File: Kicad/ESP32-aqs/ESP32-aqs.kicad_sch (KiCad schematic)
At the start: 22 parts, among them J1 UART Connector, SW1 RESET, SW2 BOOT, U1 LD1117S33TR_SOT223, U2 ESP32-WROOM-32, U3 SGP41-D-R4, U4 SX1276S8S+T-X1

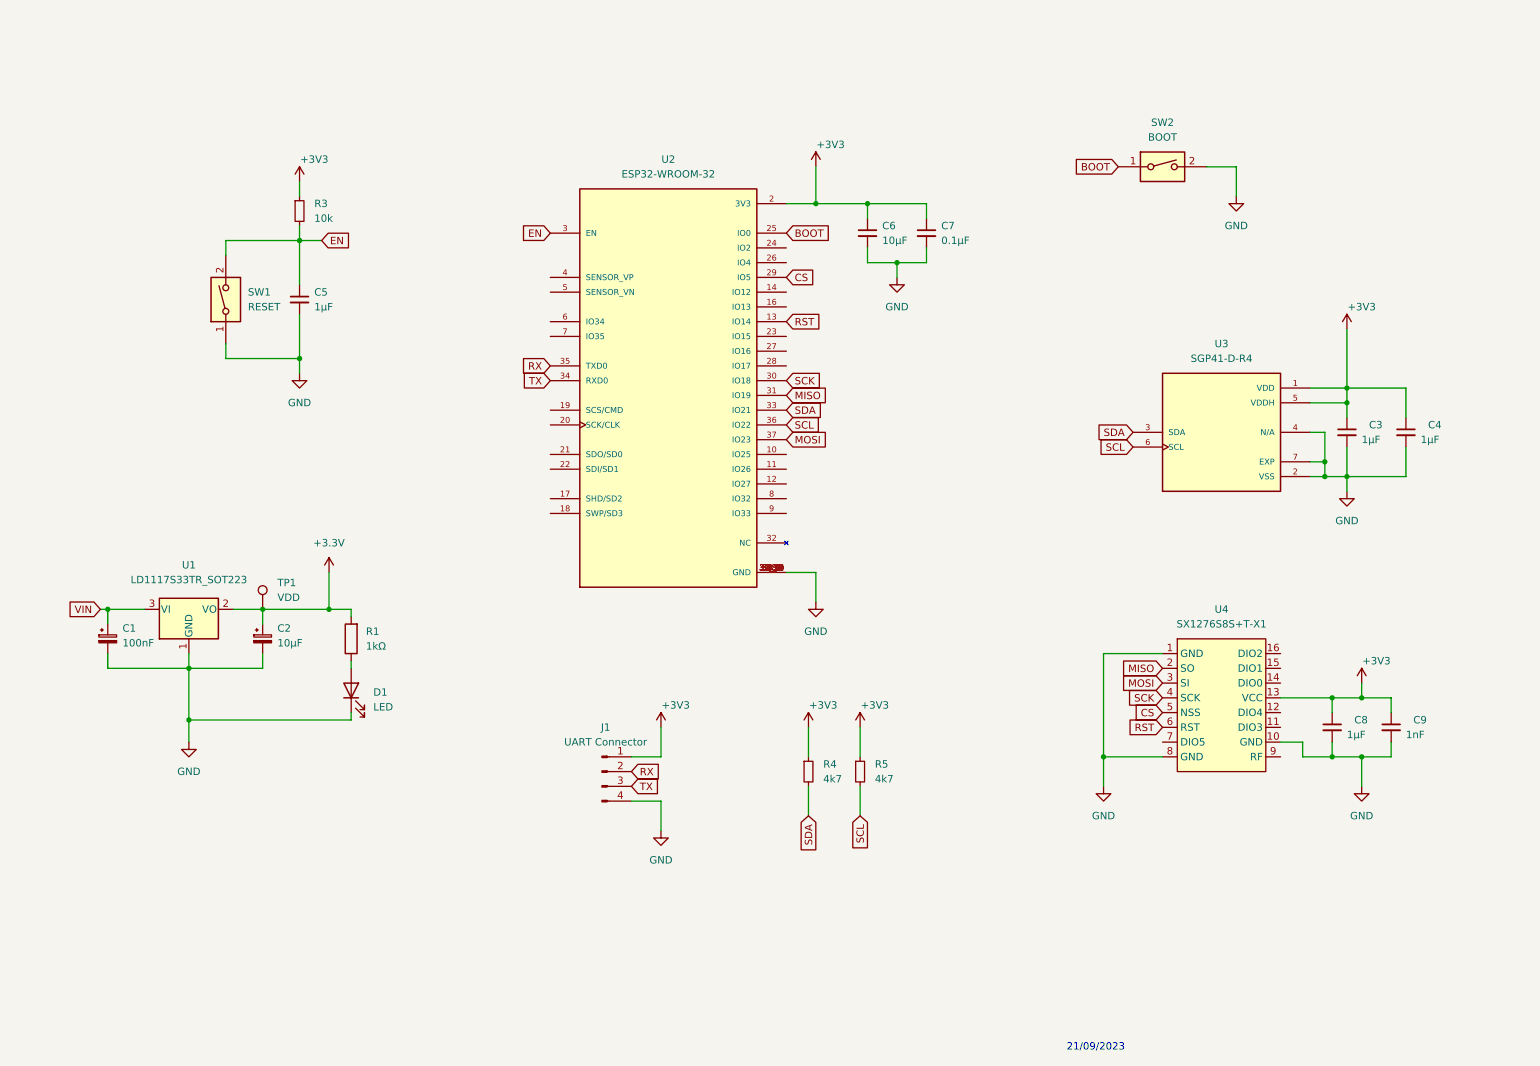
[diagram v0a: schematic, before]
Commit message: update schematic
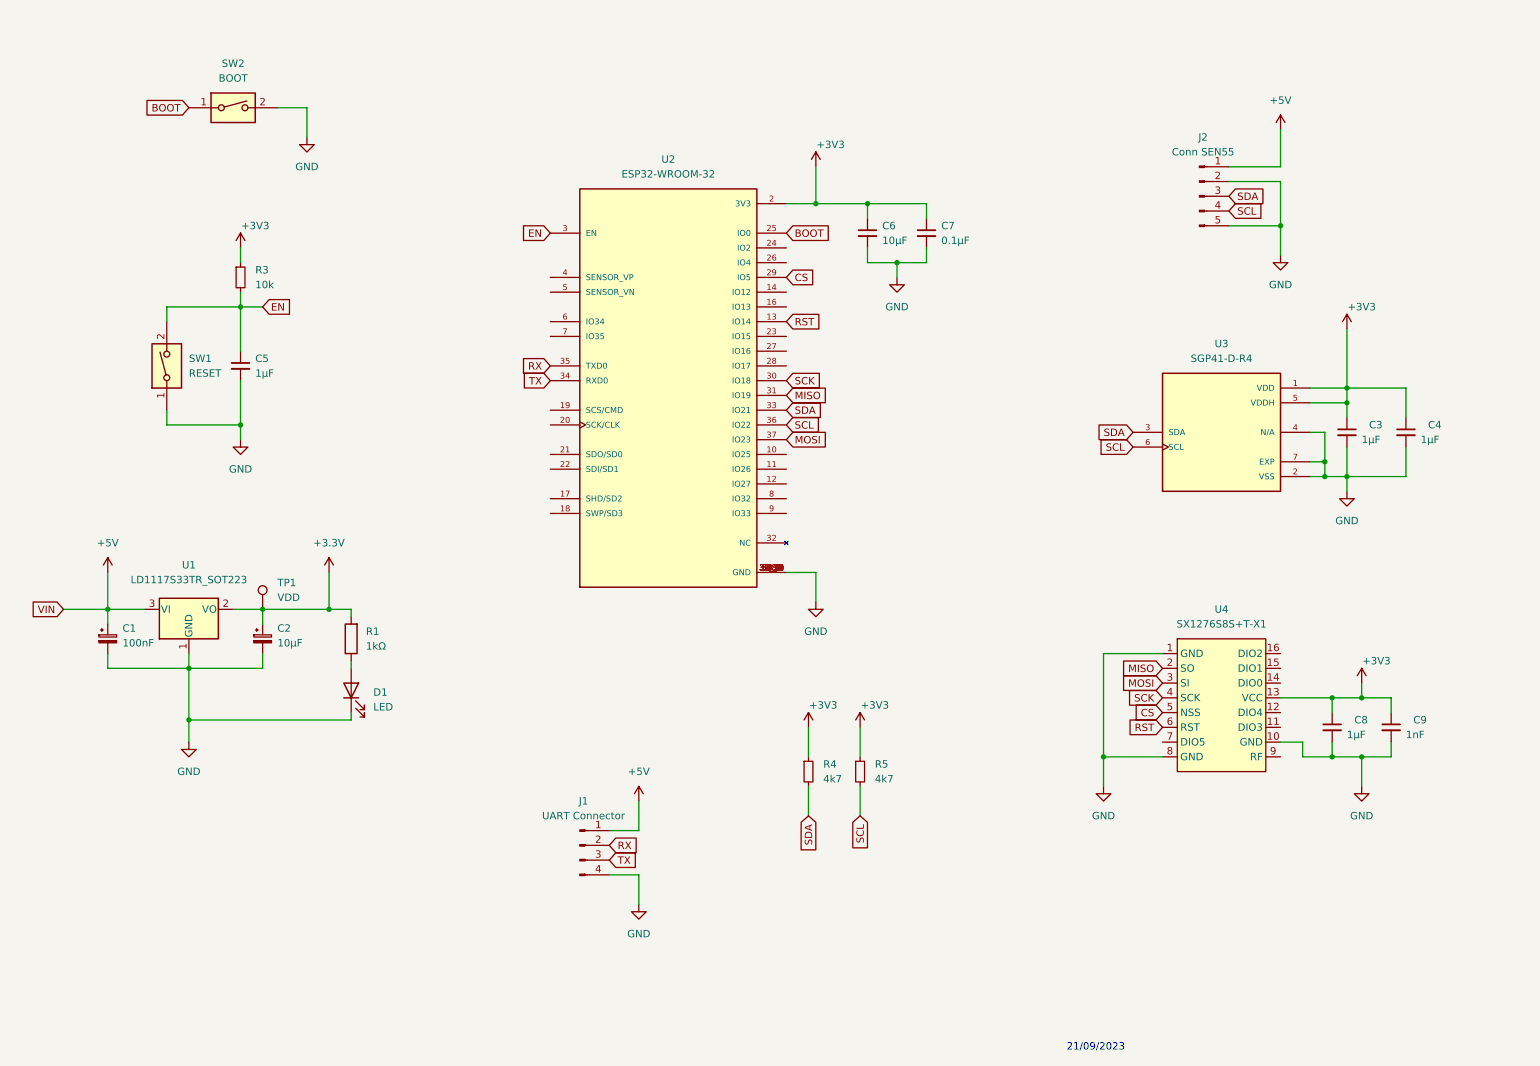
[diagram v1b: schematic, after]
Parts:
- added J2: Conn SEN55, Connector_PinHeader_2.54mm:PinHeader_1x05_P2.54mm_Vertical, symbol Connector:Conn_01x05_Male
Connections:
- net +3V3: no longer J1.1 (Pin_1)
- net GND: now also J2.2 (Pin_2), J2.5 (Pin_5)
- net SCL: now also J2.4 (Pin_4)
- net SDA: now also J2.3 (Pin_3)
- net VIN renamed +5V
- net +5V: now also J1.1 (Pin_1), J2.1 (Pin_1)
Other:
- moved on the sheet: C5, J1, R3, SW1, SW2

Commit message: Add files via upload
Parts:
- added J3: ufl connector, Connector_Coaxial:U.FL_Molex_MCRF_73412-0110_Vertical, symbol Connector:Conn_Coaxial
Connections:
- net GND: now also J3.2 (Ext)
- net at U4.9 (RF): now also J3.1 (In)
- no-connect marks 0 -> 28
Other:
- moved on the sheet: C1, C2, C5, C6, C7, C8, C9, D1, R1, R3, SW1, SW2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

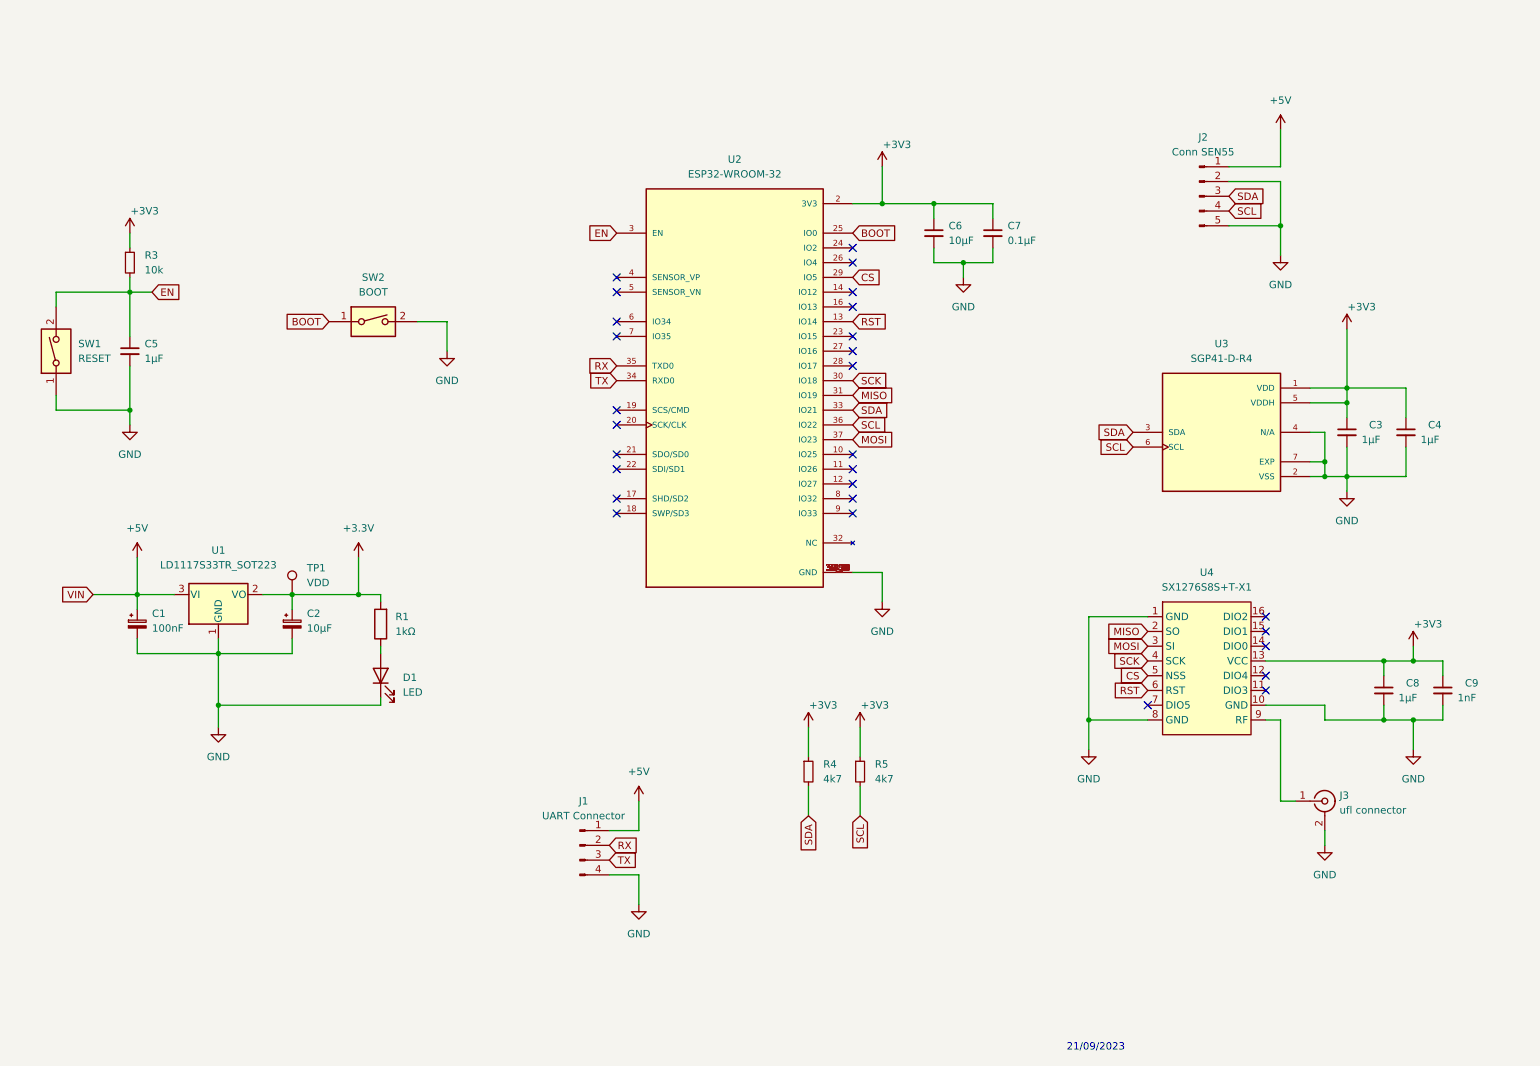
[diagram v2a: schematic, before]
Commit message: update schematic
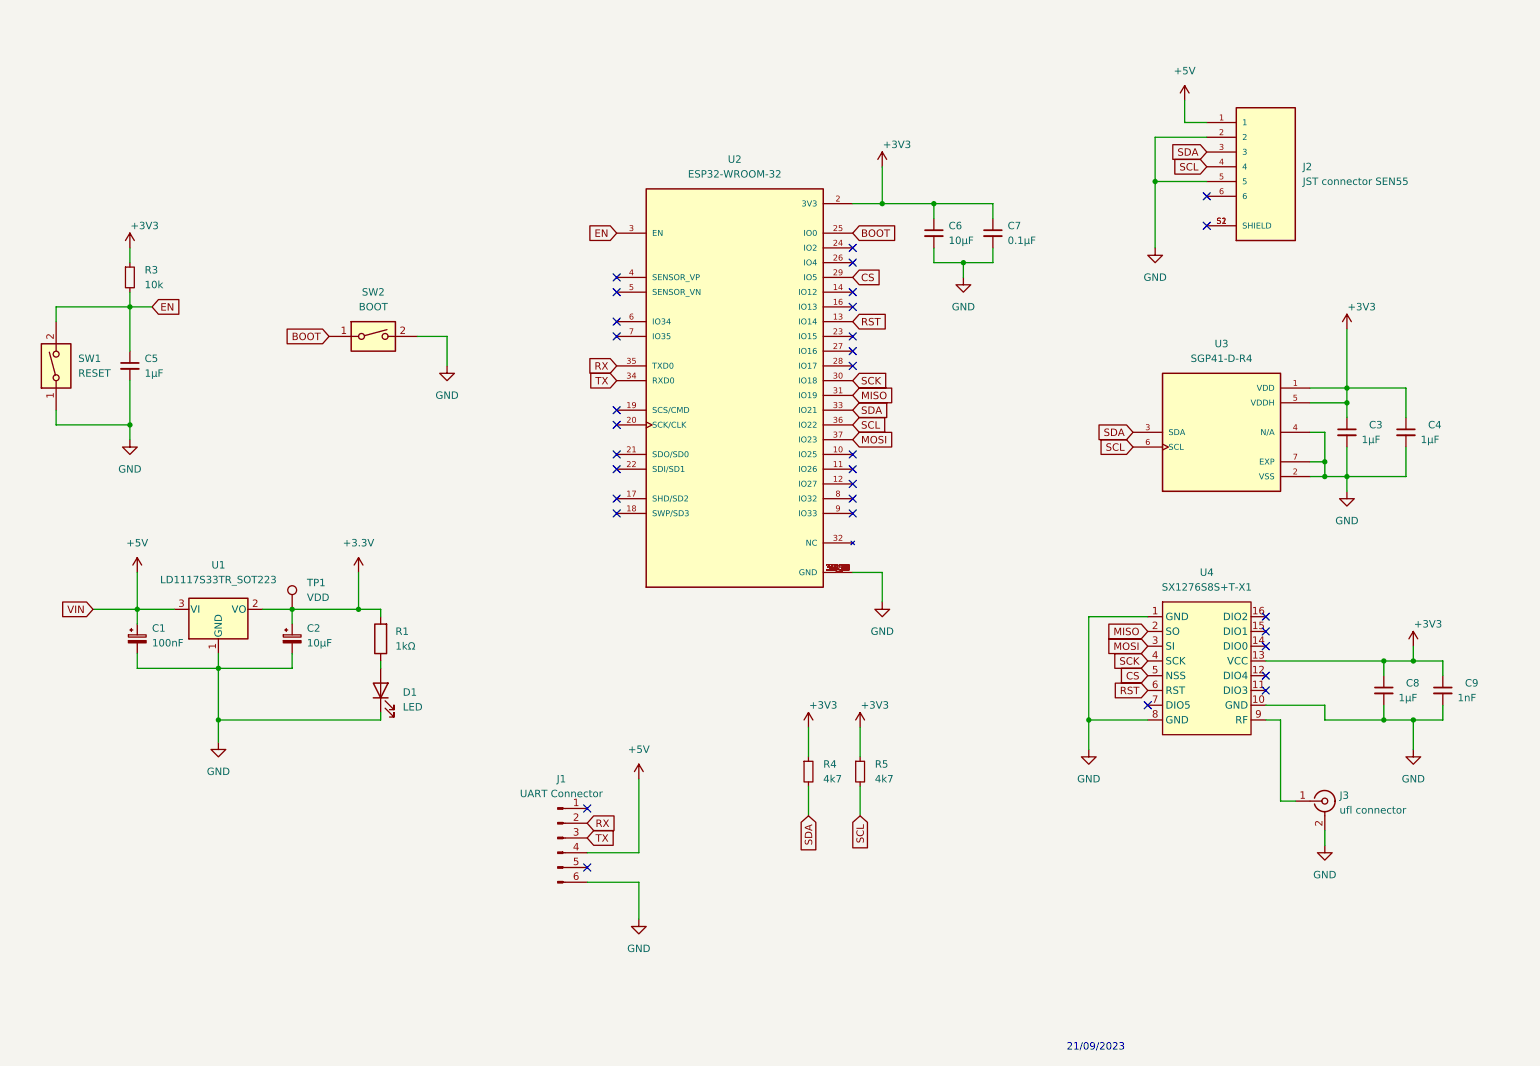
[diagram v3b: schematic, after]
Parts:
- removed J1: UART Connector, Connector_PinHeader_2.54mm:PinHeader_1x04_P2.54mm_Vertical, symbol Connector:Conn_01x04_Male
- removed J2: Conn SEN55, Connector_PinHeader_2.54mm:PinHeader_1x05_P2.54mm_Vertical, symbol Connector:Conn_01x05_Male
- added J1: UART Connector, Connector_PinHeader_2.54mm:PinHeader_1x06_P2.54mm_Vertical, symbol Connector:Conn_01x06_Male
- added J2: JST connector SEN55, ESP32-aqs:JST_BM06B-GHS-TBT_LF__SN__N_, symbol ESP32-aqs:BM06B-GHS-TBT_LF__SN__N_
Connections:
- net +5V: now also J1.4 (Pin_4), J2.1
- net GND: now also J1.6 (Pin_6), J2.2, J2.5
- net RX: now also J1.2 (Pin_2)
- net SCL: now also J2.4
- net SDA: now also J2.3
- net TX: now also J1.3 (Pin_3)
- new net: J2.S1 (SHIELD), J2.S2 (SHIELD)
- no-connect marks 28 -> 32
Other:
- moved on the sheet: C1, C2, C5, D1, R1, R3, SW1, SW2, TP1, U1

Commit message: PCB design
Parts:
- added H1, H2, H3, H4: MountingHole, MountingHole:MountingHole_2.2mm_M2_ISO7380_Pad, symbol Mechanical:MountingHole
- SW1, SW2: footprint (none) -> Button_Switch_THT:SW_PUSH_6mm_H7.3mm

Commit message: PCB design
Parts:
- added C10: 1µF, Capacitor_SMD:C_0805_2012Metric_Pad1.18x1.45mm_HandSolder, symbol Device:C_Small
- added R2: 4k7, Resistor_SMD:R_0805_2012Metric_Pad1.20x1.40mm_HandSolder, symbol Device:R_Small
- C8: value 1µF -> 100nF
- C9: value 1nF -> 1µF
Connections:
- net +3V3: no longer C9.1
- net GND: now also C9.1, C10.1; no longer C9.2
- net at J3.1 (In): now also C10.2, R2.2; no longer U4.9 (RF)
- new net ANT: C9.2, R2.1, U4.9 (RF)
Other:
- moved on the sheet: C8, J3, U4

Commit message: PCB + BoM
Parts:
- U2: LCSC (none) -> C718834
- U4: LCSC (none) -> C2844472
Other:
- moved on the sheet: C10, C3, C4, C8, C9, J2, J3, R2, U3, U4

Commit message: PCB design geupdate
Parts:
- removed H1, H3: MountingHole, MountingHole:MountingHole_2.2mm_M2_ISO7380_Pad, symbol Mechanical:MountingHole
- removed J1: UART Connector, Connector_PinHeader_2.54mm:PinHeader_1x06_P2.54mm_Vertical, symbol Connector:Conn_01x06_Male
- added J4: UART Connector, TerminalBlock_Phoenix:TerminalBlock_Phoenix_MPT-0,5-6-2.54_1x06_P2.54mm_Horizontal, symbol Connector:Screw_Terminal_01x06
- SW1: value RESET -> TC-1102-B-C-B; footprint Button_Switch_THT:SW_PUSH_6mm_H7.3mm -> Button_Switch_THT:SW_PUSH_6mm; Value2 (none) -> Reset
- SW2: value BOOT -> TC-1102-B-C-B; footprint Button_Switch_THT:SW_PUSH_6mm_H7.3mm -> Button_Switch_THT:SW_PUSH_6mm
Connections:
- net +5V: now also J4.4 (Pin_4)
- net GND: now also J4.6 (Pin_6)
- net RX: now also J4.2 (Pin_2)
- net TX: now also J4.3 (Pin_3)
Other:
- moved on the sheet: H2, H4
